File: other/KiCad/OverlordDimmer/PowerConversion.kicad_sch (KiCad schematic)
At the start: 30 parts, among them U12 AP63203WU, U13 AP63205WU

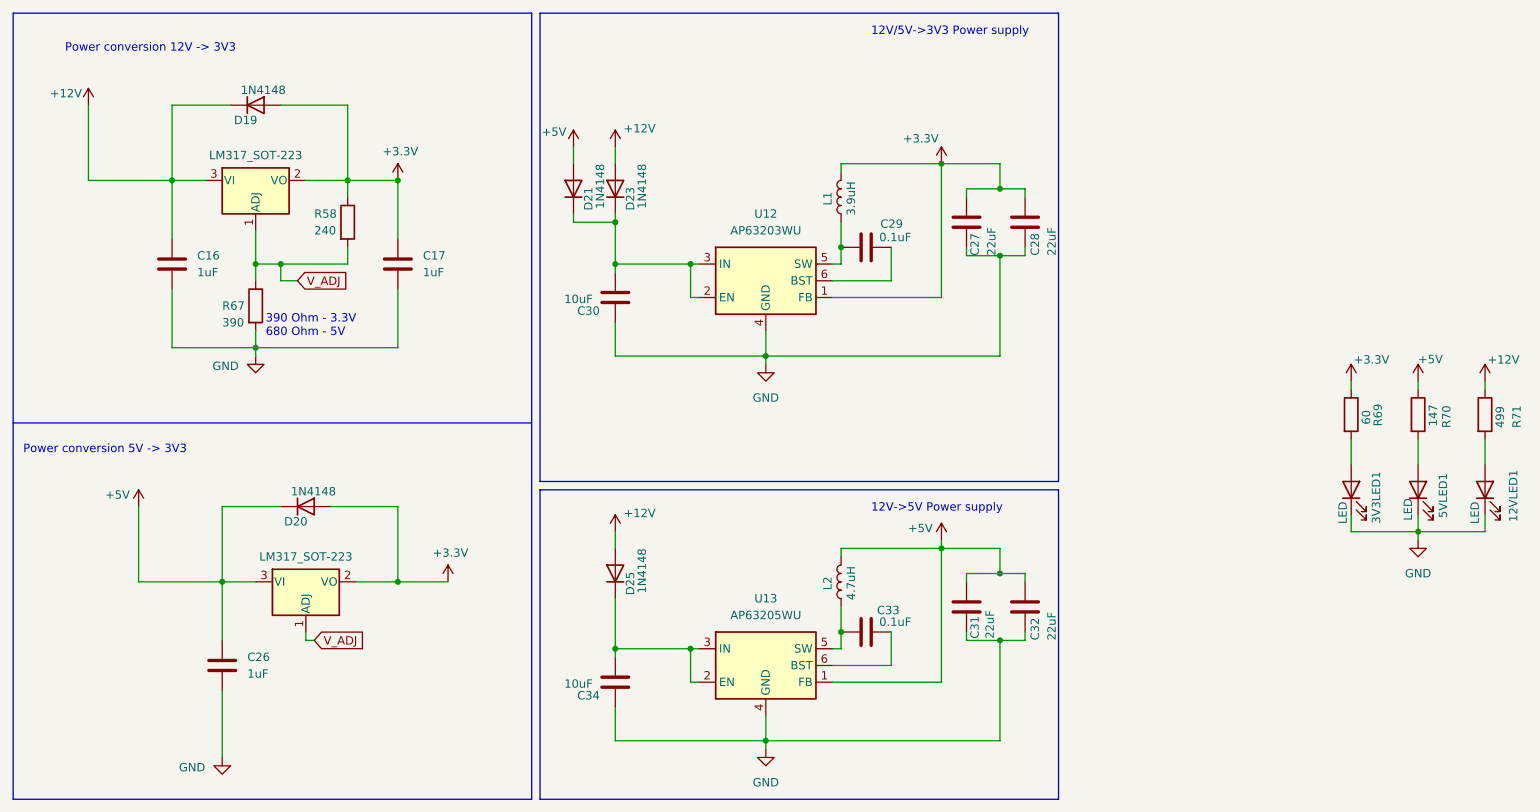
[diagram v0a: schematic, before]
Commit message: Updated PCB design - added pullup on boot pin GPIO0 - schematic cleanup - removed unused power supply parts
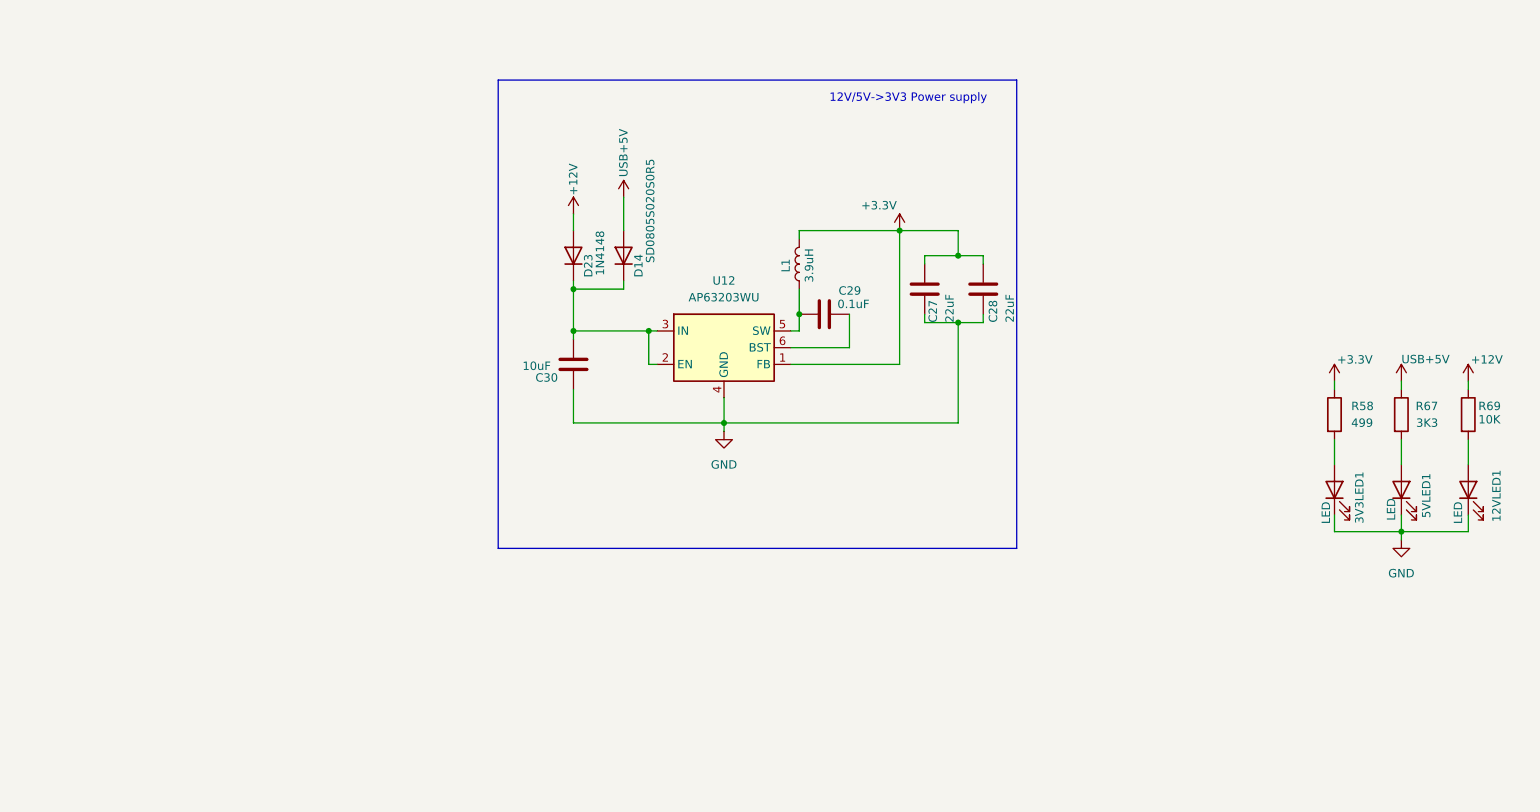
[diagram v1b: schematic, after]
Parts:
- removed C16, C17, C26: 1uF, Capacitor_SMD:C_0805_2012Metric_Pad1.18x1.45mm_HandSolder, symbol Device:C
- removed C31, C32: 22uF, Capacitor_SMD:C_0805_2012Metric_Pad1.18x1.45mm_HandSolder, symbol Device:C
- removed C33: 0.1uF, Capacitor_SMD:C_0805_2012Metric_Pad1.18x1.45mm_HandSolder, symbol Device:C
- removed C34: 10uF, Capacitor_SMD:C_0805_2012Metric_Pad1.18x1.45mm_HandSolder, symbol Device:C
- removed D19, D20, D21, D25: 1N4148, Diode_SMD:D_0805_2012Metric_Pad1.15x1.40mm_HandSolder, symbol Diode:1N4148
- removed L2: 4.7uH, Inductor_SMD:L_Bourns_SDR0604, symbol Device:L
- removed R70: 147, Resistor_SMD:R_0805_2012Metric_Pad1.20x1.40mm_HandSolder, symbol Device:R
- removed R71: 499, Resistor_SMD:R_0805_2012Metric_Pad1.20x1.40mm_HandSolder, symbol Device:R
- removed U13: AP63205WU, Package_TO_SOT_SMD:TSOT-23-6, symbol Regulator_Switching:AP63205WU
- removed U_LM317_1, U_LM317_2: LM317_SOT-223, Package_TO_SOT_SMD:SOT-223-3_TabPin2, symbol Regulator_Linear:LM317_SOT-223
- added D14: SD0805S020S0R5, Diode_SMD:D_0805_2012Metric_Pad1.15x1.40mm_HandSolder, symbol Diode:1N4148
- R58: value 240 -> 499; footprint Resistor_SMD:R_0805_2012Metric -> Resistor_SMD:R_0805_2012Metric_Pad1.20x1.40mm_HandSolder
- R67: value 390 -> 3K3; footprint Resistor_SMD:R_0805_2012Metric -> Resistor_SMD:R_0805_2012Metric_Pad1.20x1.40mm_HandSolder
- R69: value 60 -> 10K
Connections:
- net +12V: now also R69.1
- net +3.3V: no longer R69.1
- net GND: no longer R67.2
- net at C30.2, D23.1 (K), U12.2 (EN)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: now also D14.1 (K)
- net at 12VLED1.2 (A): now also R69.2
- net at 3V3LED1.2 (A): now also R58.2; no longer R69.2
- net at 5VLED1.2 (A): now also R67.2
- net V_ADJ renamed USB+5V
- net USB+5V: now also D14.2 (A); no longer R58.2
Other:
- note removed: "12V->5V Power supply"
- note removed: "390 Ohm - 3.3V 680 Ohm - 5V"
- note removed: "Power conversion 12V -> 3V3"
- note removed: "Power conversion 5V -> 3V3"
- moved on the sheet: C27, C28, C29, C30, D23, L1, U12
